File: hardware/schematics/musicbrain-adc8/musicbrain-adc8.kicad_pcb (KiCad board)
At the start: 2 copper layers, 40 x 80 mm, 23 parts, among them J1 BUS, J2 CV IN, U1 AD7606BSTZ, U2 AMS1117-5.0

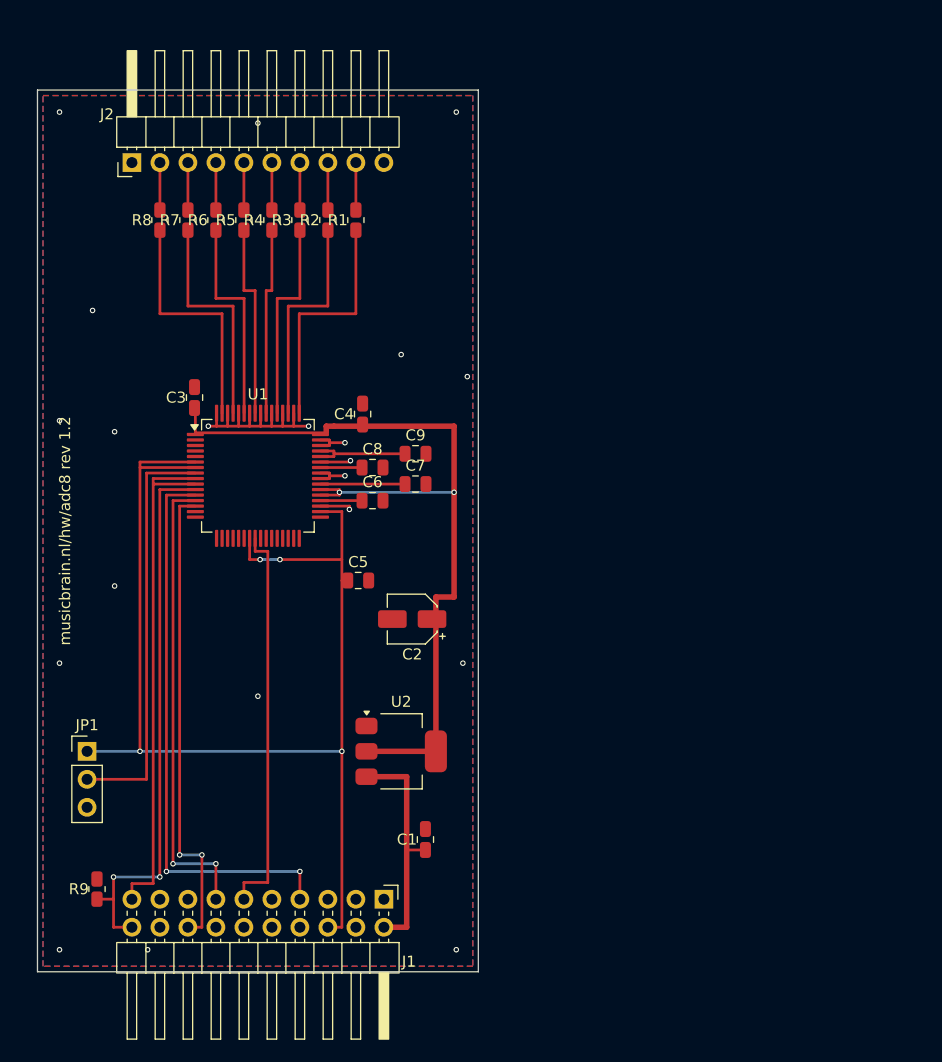
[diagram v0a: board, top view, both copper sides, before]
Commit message: adc8 gen 2: 80x45, slot 2x12, RESET lokaal, GND-binnenring
- kaart 50x80 -> 80x45; J1 2x10 -> 2x12 via bus.j1_map; pin 19 = /SPARE1
  = busbrede CONVST; J2 gecentreerd
- RESET van buslijn (SPARE2, vervallen in gen 2) naar lokale RC-power-up:
  C15 100n vanaf +3V3 + R9 100k pulldown (tau 10 ms)
- U1 rot 0: V-ingangen noord naar de IN-kolommen; v1.2-mapping (jack j =
  V(9-j), remap in MbAdc8) blijft
- GND-binnenring onder de LQFP: zone-vulling bereikt 0,5mm-pads nooit
  (0,6 mm kanaal nodig); straps + ring + 2 via's, zoals gen-1 met de hand
- prep_dsn --route-gnd: GND blijft routeerbaar net (alleen planes eruit),
  zodat freerouting de vaste GND-wiring ziet en zelf GND afmaakt
- gen_adc_pcb.py (cardlib) vervangt gen_adc_pcb_v11.py + oude gen_adc_pcb.py
- ERC 0, netcheck OK, DRC 0/0

Co-Authored-By: Claude Fable 5 <noreply@anthropic.com>
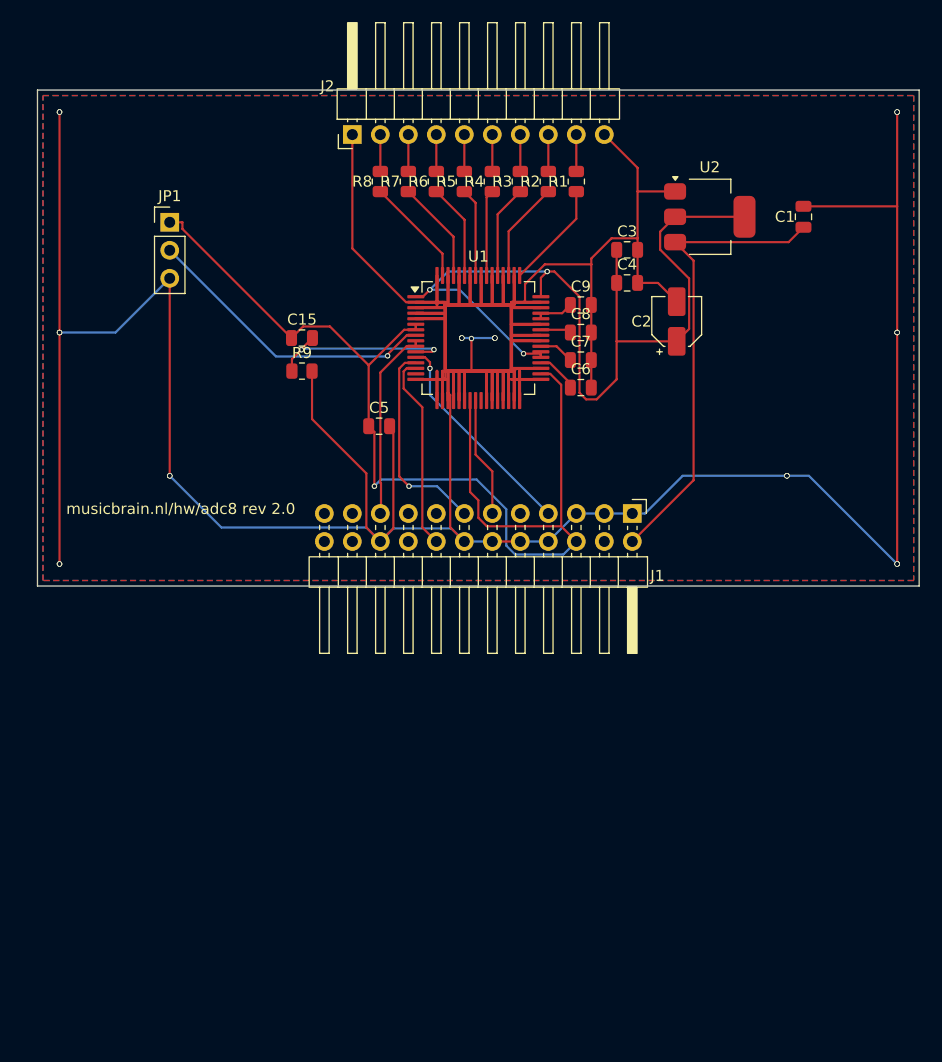
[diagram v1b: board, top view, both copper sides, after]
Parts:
- added C15: 100n, Capacitor_SMD:C_0805_2012Metric, F.Cu at (124.0, 122.5)
- J1: footprint Connector_PinHeader_2.54mm:PinHeader_2x10_P2.54mm_Horizontal -> Connector_PinHeader_2.54mm:PinHeader_2x12_P2.54mm_Horizontal
- moved C1 66.1 mm to (169.5, 111.5)
- moved U2 56.0 mm to (161.0, 111.5)
- moved R9 50.5 mm to (124.0, 125.5), turned to 0 degrees
- moved JP1 48.6 mm to (112.0, 112.0)
- moved J1 41.6 mm to (154.0, 138.4)
- moved C3 41.5 mm to (153.5, 114.5), turned to 0 degrees
- moved C2 36.1 mm to (158.0, 121.0), turned to 90 degrees
- moved C4 26.8 mm to (153.5, 117.5), turned to 0 degrees
- moved U1 23.6 mm to (140.0, 122.5)
- moved C8 22.5 mm to (149.3, 122.0)
- moved C6 21.5 mm to (149.3, 127.0)
- moved R4 20.3 mm to (141.3, 108.3)
- moved R8 20.3 mm to (131.1, 108.3)
- moved R1 20.3 mm to (148.9, 108.3)
- moved R2 20.3 mm to (146.3, 108.3)
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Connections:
- net Net-(U1-REFCAPA) renamed /REFCAP
- net Net-(U1-REFIN/REFOUT) renamed /REF
- net Net-(U1-REGCAP1) renamed /REGCAP1
- net Net-(U1-REGCAP2) renamed /REGCAP2
- net Net-(U1-V1) renamed /V1
- net Net-(U1-V2) renamed /V2
- net Net-(U1-V3) renamed /V3
- net Net-(U1-V4) renamed /V4
- net Net-(U1-V5) renamed /V5
- net Net-(U1-V6) renamed /V6
- net Net-(U1-V7) renamed /V7
- net Net-(U1-V8) renamed /V8
- J1 pad 20: /RESET -> GND
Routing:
- net GND: track 31.4 -> 537.6 mm
- net /RESET: track 50.3 -> 17.6 mm
- net /SCLK: track 51.4 -> 19.6 mm, vias 2 -> 1
- net /CONVST: track 47.8 -> 18.0 mm
- net /MISO: track 36.1 -> 10.9 mm
- net /IRQ: track 42.9 -> 17.9 mm, vias 2 -> 0
- net /CS: track 42.1 -> 18.8 mm, vias 2 -> 1
- net +12V: track 21.1 -> 42.4 mm
- net /V8: track 22.3 -> 9.95 mm
- net /V1: track 21.8 -> 9.74 mm
- net /V7: track 20.7 -> 9.31 mm
- net /V2: track 20.2 -> 9.10 mm
- net /V6: track 19.2 -> 8.67 mm
- net /RANGE: track 37.6 -> 27.2 mm, vias 0 -> 1
- net /V3: track 18.7 -> 8.47 mm
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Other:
- board size 40 x 80 mm -> 80 x 45 mm
- board text added: "musicbrain.nl/hw/adc8 rev 2.0"
- board text removed: "musicbrain.nl/hw/adc8 rev 1.2"

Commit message: afslank-ronde: potriser 40, gatein8 50, gate8 55, dac8 60, adc8 65 (x45)
80 mm was een maximum, geen eis (observatie Mark): J1/J2 blijven op de
hartlijn, de rand schuift naar binnen. Silk verticaal in de westrand
(horizontaal paste niet meer); hoekvia's geparametriseerd op BX0/BX1;
zwervers mee (gate8 C1, dac8 C3, adc8 JP1). Alle vijf opnieuw geroute
(verse SES) en op ERC 0 + netcheck OK + DRC 0/0.

Co-Authored-By: Claude Fable 5 <noreply@anthropic.com>
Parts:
- moved JP1 2.00 mm to (114.0, 112.0)
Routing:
- net GND: track 537.6 -> 507.8 mm, vias 21 -> 20
- net +3V3: track 102.1 -> 85.6 mm, vias 1 -> 2
- net +5V: track 83.3 -> 72.5 mm, vias 3 -> 2
- net /SCLK: track 19.6 -> 24.1 mm
- net /CS: track 18.8 -> 16.0 mm
- net /REFCAP: track 3.99 -> 5.16 mm
- net /IRQ: track 17.9 -> 18.9 mm
- net +12V: track 42.4 -> 41.7 mm
- net /RESET: track 17.6 -> 18.3 mm
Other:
- board size 80 x 45 mm -> 65 x 45 mm
